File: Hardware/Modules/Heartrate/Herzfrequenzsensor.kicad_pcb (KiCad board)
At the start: 2 copper layers, 35 x 35 mm, 26 parts, among them J4 B4B-EH-A, J5 B4B-EH-A, J6 Conn_01x01_Pin, U6 MAX30101EFD_T, U7 PCA9306DCTR, U8 MAX32664GTGA_T, U9 TLV70018_SOT23-5

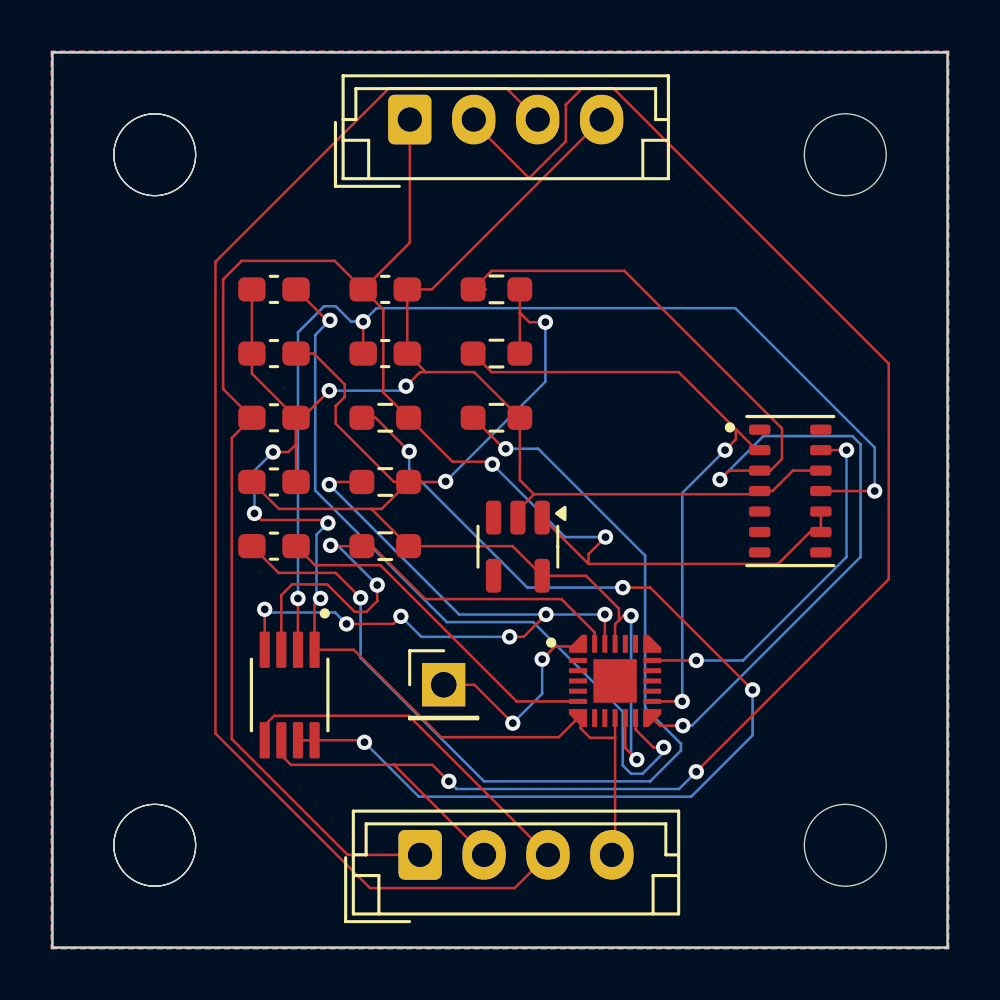
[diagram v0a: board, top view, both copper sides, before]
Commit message: Add Text to Heart-Rate, finish Flight-ModuleV1
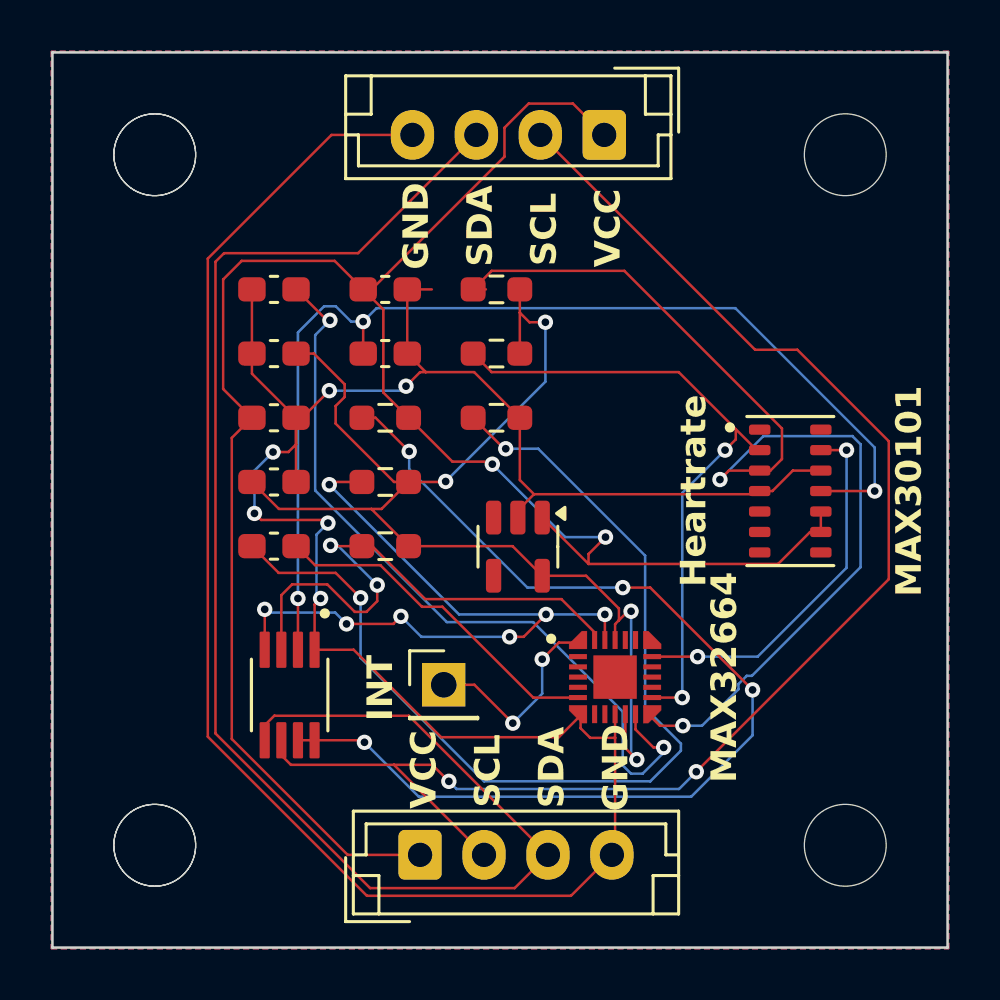
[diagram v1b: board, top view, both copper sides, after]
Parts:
- moved J4 7.62 mm to (140.7, 48.8), turned to 180 degrees
- moved U8 0.15 mm to (141.1, 70.0)
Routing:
- net VCORE: track 81.0 -> 119.4 mm
- net SCL: track 65.7 -> 57.2 mm
- net VCC: track 71.3 -> 77.5 mm
- net SDA: track 64.5 -> 60.8 mm
- net B3: track 41.3 -> 41.8 mm
- added copper zone on F.Cu, net VCORE
- removed copper zone on F.Cu, net VCC
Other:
- board text added: "GND"
- board text added: "Heartrate"
- board text added: "INT"
- board text added: "MAX30101"
- board text added: "MAX32664"
- board text added: "SCL"
- board text added: "SDA"
- board text added: "VCC"

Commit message: Finishing Modules
Wifi-Module
Flight-Module
REPAIR:
- Heartrate
- Flight-Module
- Wifi-Module
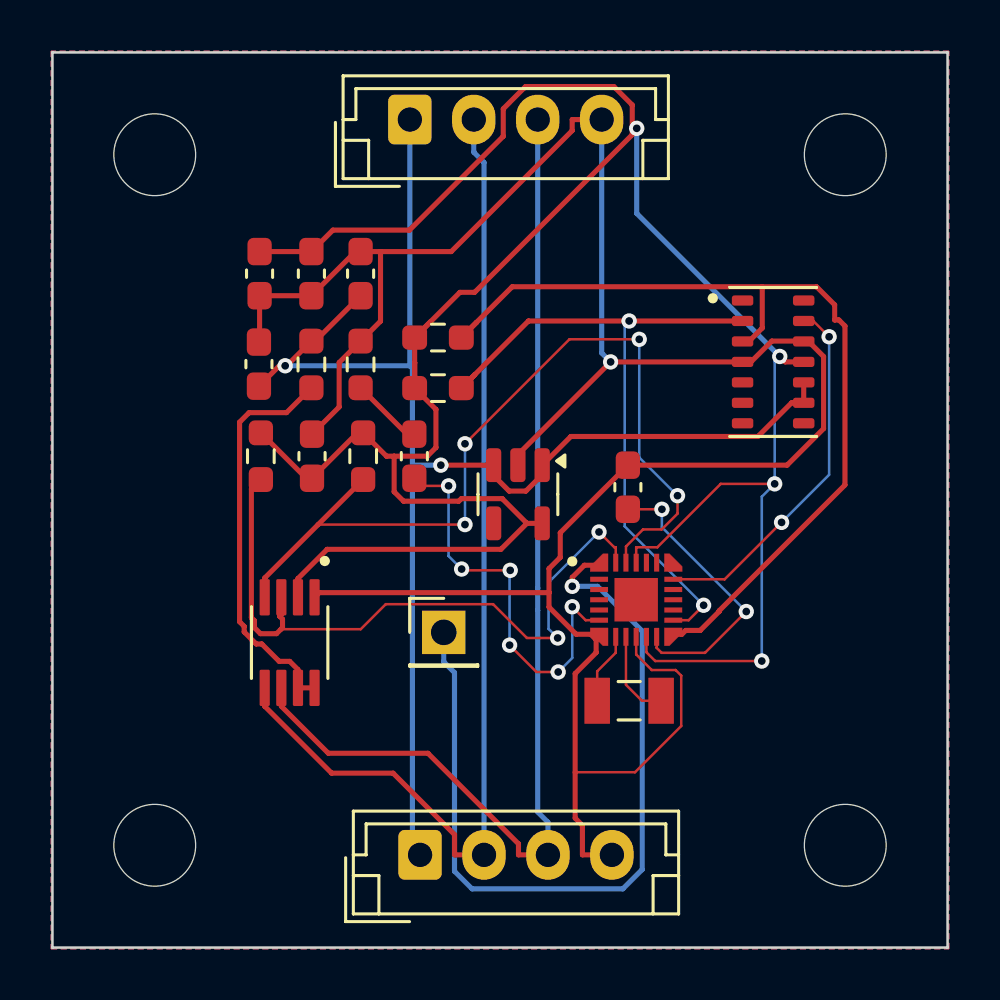
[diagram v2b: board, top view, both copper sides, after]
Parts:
- removed ? (x2): , 
- added Y1: 32KHz, Modular-Electronics-Toolkit-BP:XTAL_CM7V-T1A-LOW-ESR-32.768KHZ-6PF-20-TA-QC, F.Cu at (141.7, 71.0)
- moved C6 15.9 mm to (141.6, 62.6), turned to -90 degrees
- moved J4 7.62 mm to (133.1, 48.2), turned to 0 degrees
- moved C10 6.52 mm to (133.3, 61.4), turned to -90 degrees
- moved R5 6.00 mm to (127.3, 61.4), turned to 90 degrees
- moved R8 5.71 mm to (131.2, 57.8), turned to 90 degrees
- moved U6 5.09 mm to (147.3, 57.7)
- moved C12 4.25 mm to (129.2, 54.2), turned to -90 degrees
- moved R3 3.56 mm to (129.2, 57.8), turned to 90 degrees
- moved C7 3.18 mm to (127.2, 54.2), turned to 90 degrees
- moved U8 3.14 mm to (141.9, 67.0)
- moved R6 2.96 mm to (134.2, 56.8), turned to 180 degrees
- moved R7 2.66 mm to (134.2, 58.7), turned to 180 degrees
- moved C8 2.18 mm to (127.2, 57.8), turned to 90 degrees
- moved J6 2.05 mm to (134.4, 68.3)
- moved U7 2.05 mm to (128.4, 68.7)
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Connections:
- C12 pad 1: VREF -> V18
- J4 pad 2: SCL -> SDA
- J4 pad 3: SDA -> SCL
- J5 pad 2: SCL -> SDA
- J5 pad 3: SDA -> SCL
- U6 pad 11: VREF -> V18
- U7 pad 2: VREF -> V18
- U8 pad 8: unconnected-(U8-32KOUT-Pad8) -> Net-(U8-32KOUT)
- U8 pad 9: unconnected-(U8-32KIN-Pad9) -> Net-(U8-32KIN)
- U9 pad 3: unconnected-(U9-EN-Pad3) -> VCC
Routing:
- net V18: track 49.0 -> 101.8 mm
- net VREF: track 43.2 -> 0.00 mm, vias 3 -> 0
- net Net-(C10-Pad1): track 39.6 -> 2.85 mm, vias 2 -> 0
- net Net-(U7-EN): track 41.6 -> 15.7 mm, vias 4 -> 0
- net J1: track 8.13 -> 31.9 mm, vias 2 -> 1
- net VCC: track 77.5 -> 57.6 mm
- net SDA: track 60.8 -> 41.1 mm
- net VCORE: track 119.4 -> 100.1 mm, vias 6 -> 1
- net Net-(U8-VCORE): track 30.5 -> 11.4 mm
- net SCL: track 57.2 -> 42.7 mm, vias 2 -> 0
- net B3: track 41.8 -> 35.7 mm, vias 2 -> 0
- net B1: track 29.0 -> 34.2 mm, vias 7 -> 4
- net B2: track 22.0 -> 26.9 mm
- net Net-(U8-32KIN): track 0.00 -> 3.51 mm
- net Net-(U8-32KOUT): track 0.00 -> 2.80 mm
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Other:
- board text removed: "GND"
- board text removed: "Heartrate"
- board text removed: "INT"
- board text removed: "MAX30101"
- board text removed: "MAX32664"
- board text removed: "SCL"
- board text removed: "SDA"
- board text removed: "VCC"

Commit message: Pushing Final Versions of all Modules (2025)
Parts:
- Y1: footprint Modular-Electronics-Toolkit-BP:XTAL_CM7V-T1A-LOW-ESR-32.768KHZ-6PF-20-TA-QC -> Modular-Elektronics-Toolkit-Global-Libary:XTAL_CM7V-T1A-LOW-ESR-32.768KHZ-6PF-20-TA-QC
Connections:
- net VCORE renamed GND
